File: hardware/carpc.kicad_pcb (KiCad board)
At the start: 2 copper layers, 105.4 x 67.6 mm, 47 parts, among them IC1 ATMEGA328-P, K3 CANBus, P1 PWR_IN, P2 MELBUS, P3 CONN_4, P4 RTI, P5 RELAY_OUT, Q1 BC547, Q2 RELAY, Q3 BC547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

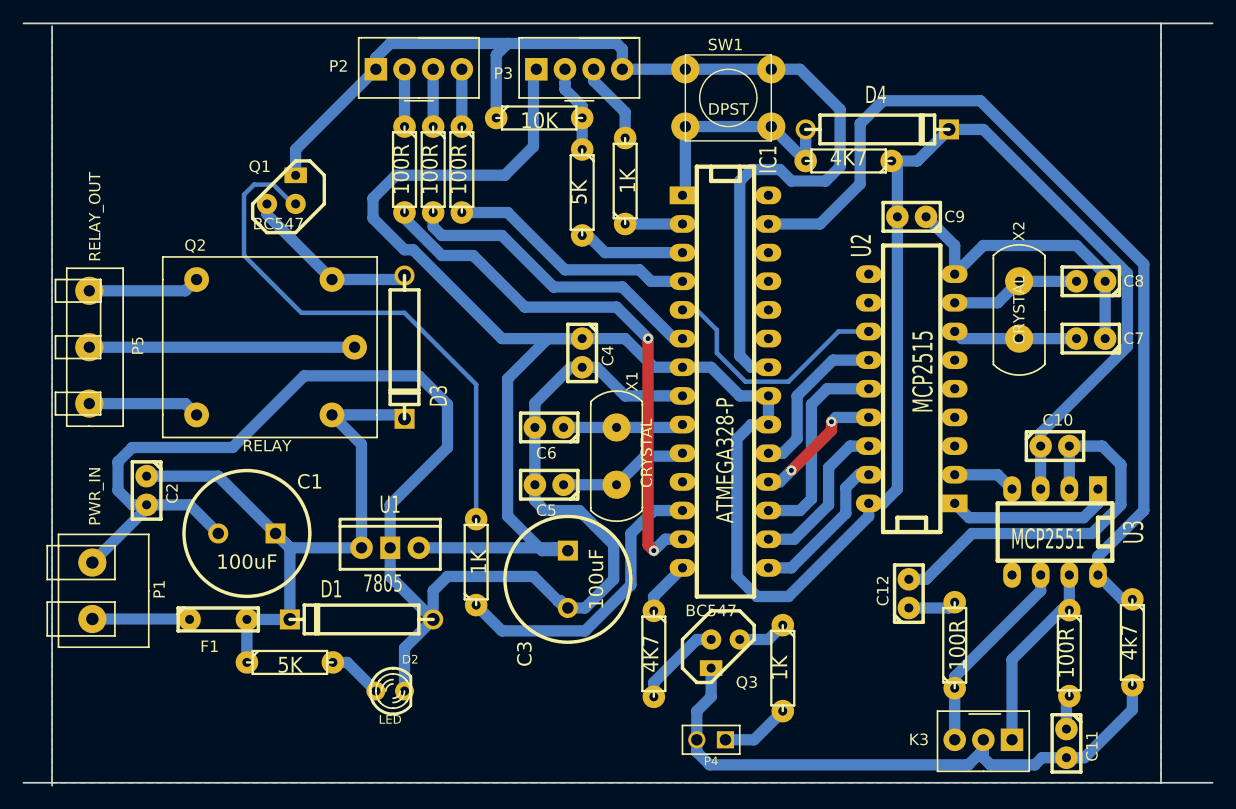
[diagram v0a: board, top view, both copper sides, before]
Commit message: Fixed an error with transistor pinout (it can be fixed easily by swapping both TO-92 transistors
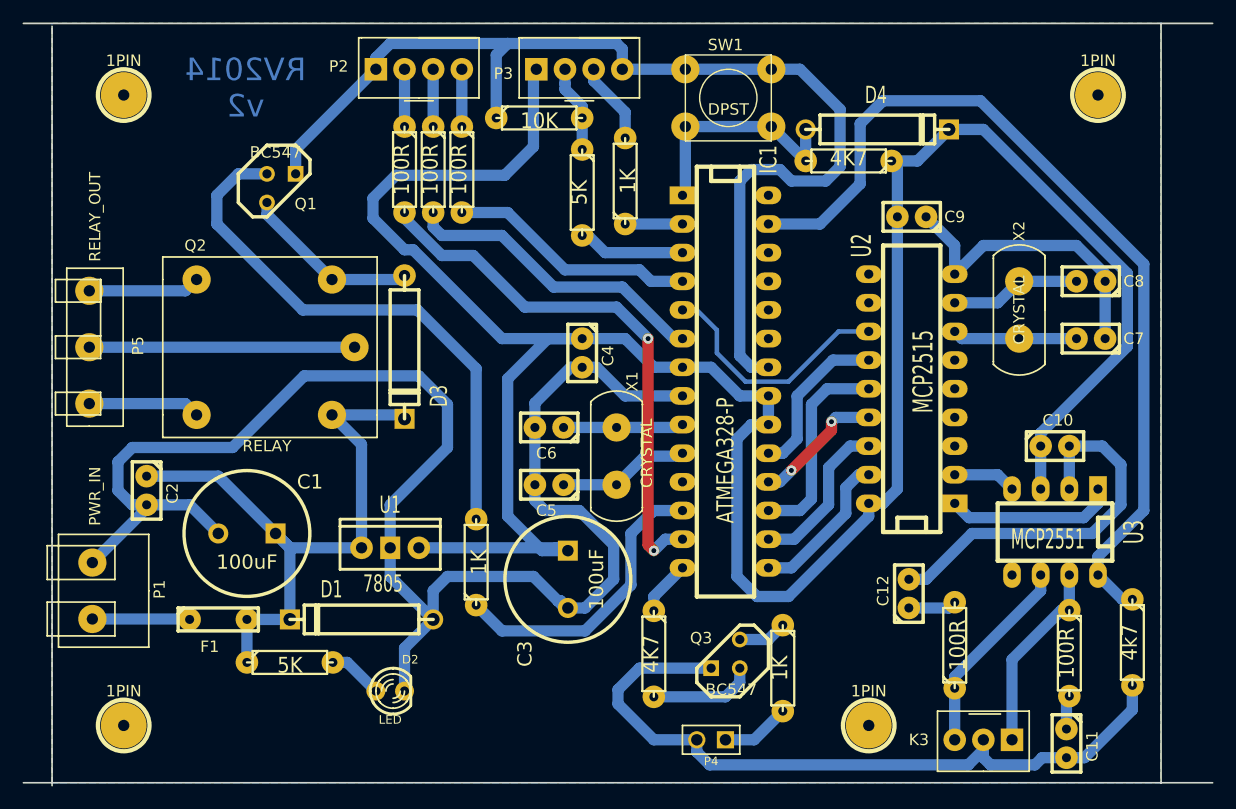
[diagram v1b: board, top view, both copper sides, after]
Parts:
- added 1PIN: P***, 1pin, F.Cu at (68.6, 53.3)
- added 1PIN: P***, 1pin, F.Cu at (134.6, 109.2)
- added 1PIN: P***, 1pin, F.Cu at (68.6, 109.2)
- added 1PIN: P***, 1pin, F.Cu at (154.9, 53.3)
- Q1, Q3: footprint TO92-CBE -> TO92-EBC
- moved Q1 0.13 mm to (82.5, 61.6), turned to 0 degrees
- turned Q3 to 180 degrees
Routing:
- net GND: track 356.5 -> 368.2 mm
- net N-0000037: track 7.93 -> 9.42 mm
- net N-0000013: track 48.3 -> 49.4 mm
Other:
- board text added: "RV2014 v2"
